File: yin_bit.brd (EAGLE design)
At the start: 51 x 22 mm, 16 parts, among them CN1 3p-2.54, J1 4P-2.0, Q1 CJ2305, SW1 MK-12C02 G1.5, U1 SN74LVC1G125DCKR-SC70-5, U2 LP2985-33DBVR

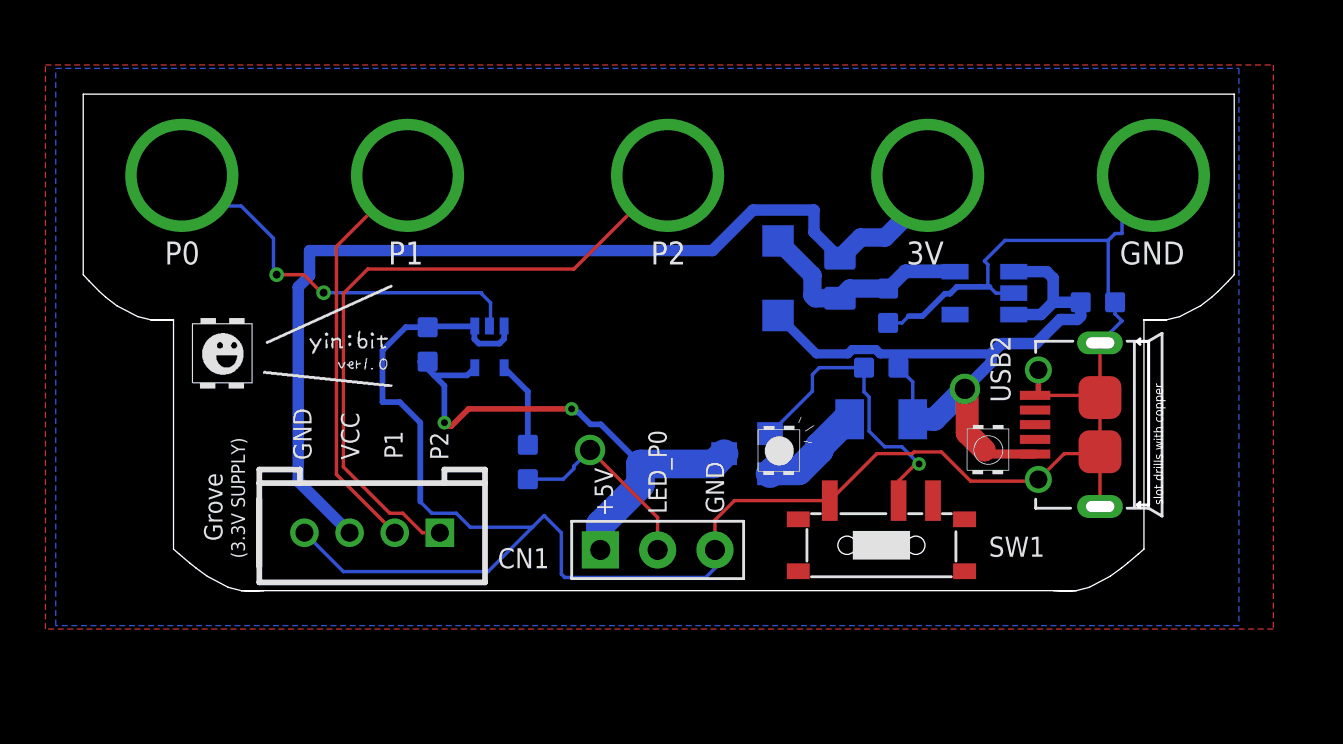
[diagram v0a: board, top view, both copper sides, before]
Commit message: 基板サイズ修正
基板サイズを修正、USBの干渉問題
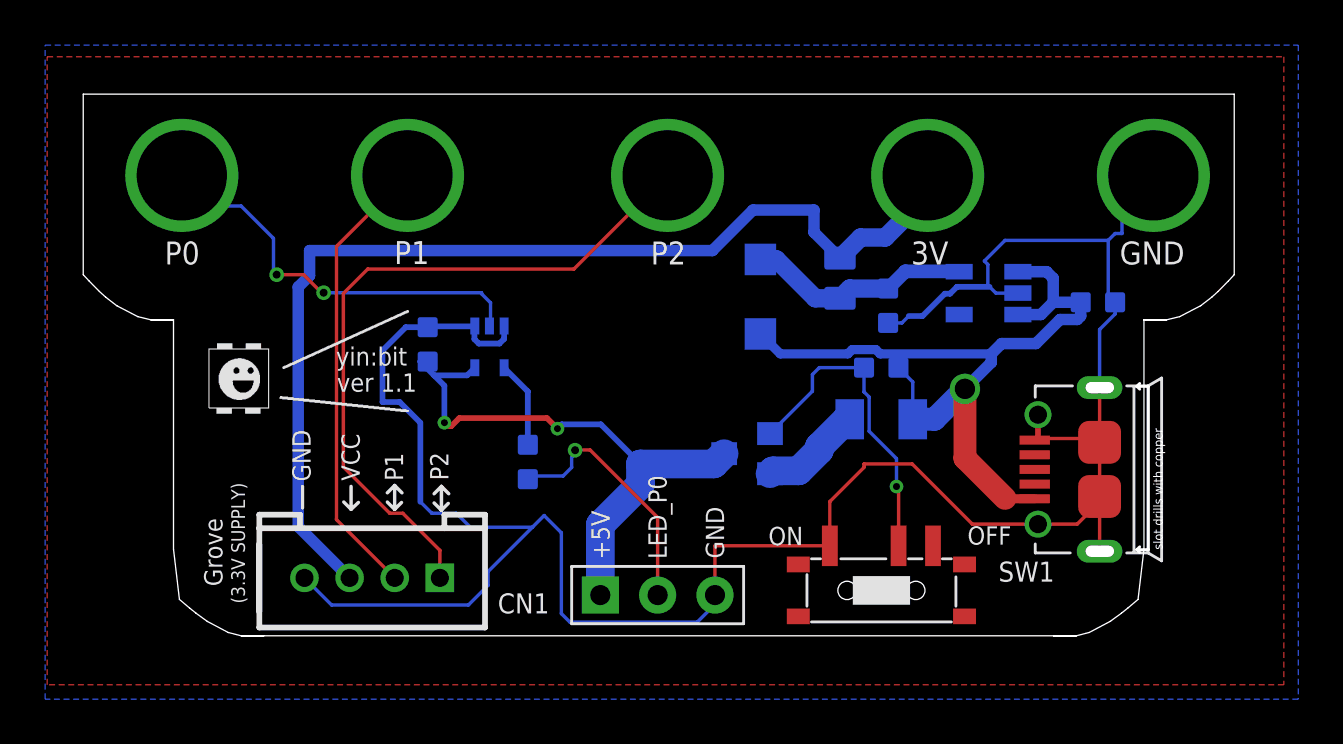
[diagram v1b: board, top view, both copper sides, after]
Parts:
- moved CN1 2.00 mm to (44.7, 20.4)
- moved J1 2.00 mm to (32.0, 21.2)
- moved SW1 2.00 mm to (54.6, 20.6)
- moved USB2 1.98 mm to (64.2, 26.0)
- moved D1 1.13 mm to (49.2, 33.6)
- moved U2 0.18 mm to (59.3, 33.8)
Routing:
- net GND: track 98.8 -> 105.6 mm
- net N$3: track 9.03 -> 11.3 mm
- net P1: track 18.2 -> 20.2 mm
- net +3V3: track 45.3 -> 47.3 mm
- net +5V: track 23.9 -> 25.8 mm
- net VCC: track 34.5 -> 36.1 mm
- net P2: track 29.7 -> 31.2 mm
- net N$4: track 13.6 -> 14.3 mm
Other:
- board size 51 x 22 mm -> 51 x 24 mm
- board text added: "@hirowo556"
- board text added: "OFF"
- board text added: "ON"
- board text added: "ver 1.1"
- board text added: "yin:bit"
